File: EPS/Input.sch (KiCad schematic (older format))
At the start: 3 parts

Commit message: Updated schematics
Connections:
- wire segments 40 -> 44
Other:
- note removed: "OpAmp feedback control here (or in own sheet)"
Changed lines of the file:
@@
 LIBS:max40200
 LIBS:tps7a7002
+LIBS:max5395
 LIBS:EPS-cache
 EELAYER 25 0
@@
 S 5150 1625 1300 1150
 U 5A812530
-F0 "Boost_converters" 60
+F0 "Boost_converters with digi pot" 60
 F1 "Boost_converters.sch" 60
 F2 "BOOST1_IN" I L 5150 1775 60
@@
 Text Notes 6475 2550 0    60   ~ 0
 To ADC
-Text Notes 4900 4000 0    60   ~ 0
-OpAmp feedback control here (or in own sheet)
-Text GLabel 5000 2400 0    60   Input ~ 0
-DAC1
-Text GLabel 5000 2525 0    60   Input ~ 0
-DAC2
-Text GLabel 5000 2650 0    60   Input ~ 0
-DAC3
 Text GLabel 6575 5525 1    60   Output ~ 0
 DAC1
@@
 	5775 6450 5775 6350
 Wire Wire Line
-	5775 4625 5775 5650
+	5775 4625 5775 4950
+Wire Wire Line
+	5775 4950 5775 5350
+Wire Wire Line
+	5775 5350 5775 5650
 Wire Wire Line
 	5775 5350 5825 5350
@@
 	8625 2025 8850 2025
 Wire Wire Line
-	8850 2025 8850 1775
-Wire Wire Line
-	8625 1775 9000 1775
+	8850 2025 8850 1900
+Wire Wire Line
+	8850 1900 8850 1775
+Wire Wire Line
+	8625 1775 8850 1775
+Wire Wire Line
+	8850 1775 9000 1775
 Connection ~ 8850 1775
 Wire Wire Line
 	8625 1900 8850 1900
 Connection ~ 8850 1900
-Wire Notes Line
-	4850 2825 4850 3700
-Wire Notes Line
-	4850 3700 5775 3700
-Wire Notes Line
-	5775 3700 5775 3800
-Wire Notes Line
-	6850 4100 6850 5000
-Wire Notes Line
-	6850 5000 6675 5000
-Wire Notes Line
-	6675 5000 6675 5125
 $EndSCHEMATC

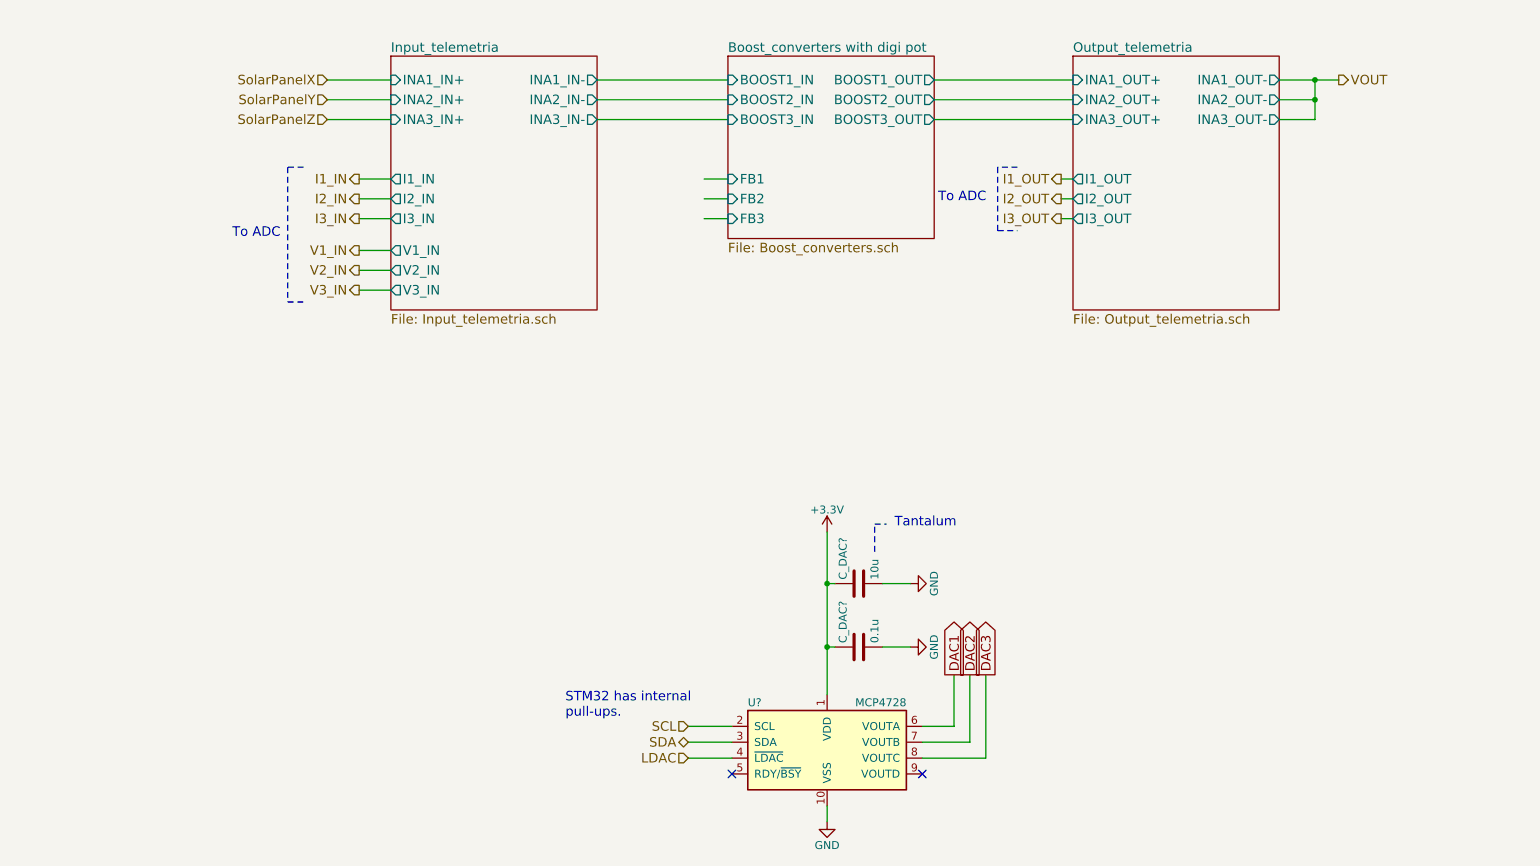
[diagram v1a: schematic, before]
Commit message: Updated Schematics
Added:
- digital pot
- digital loads
- updated  switch sheet to block two ways before battery
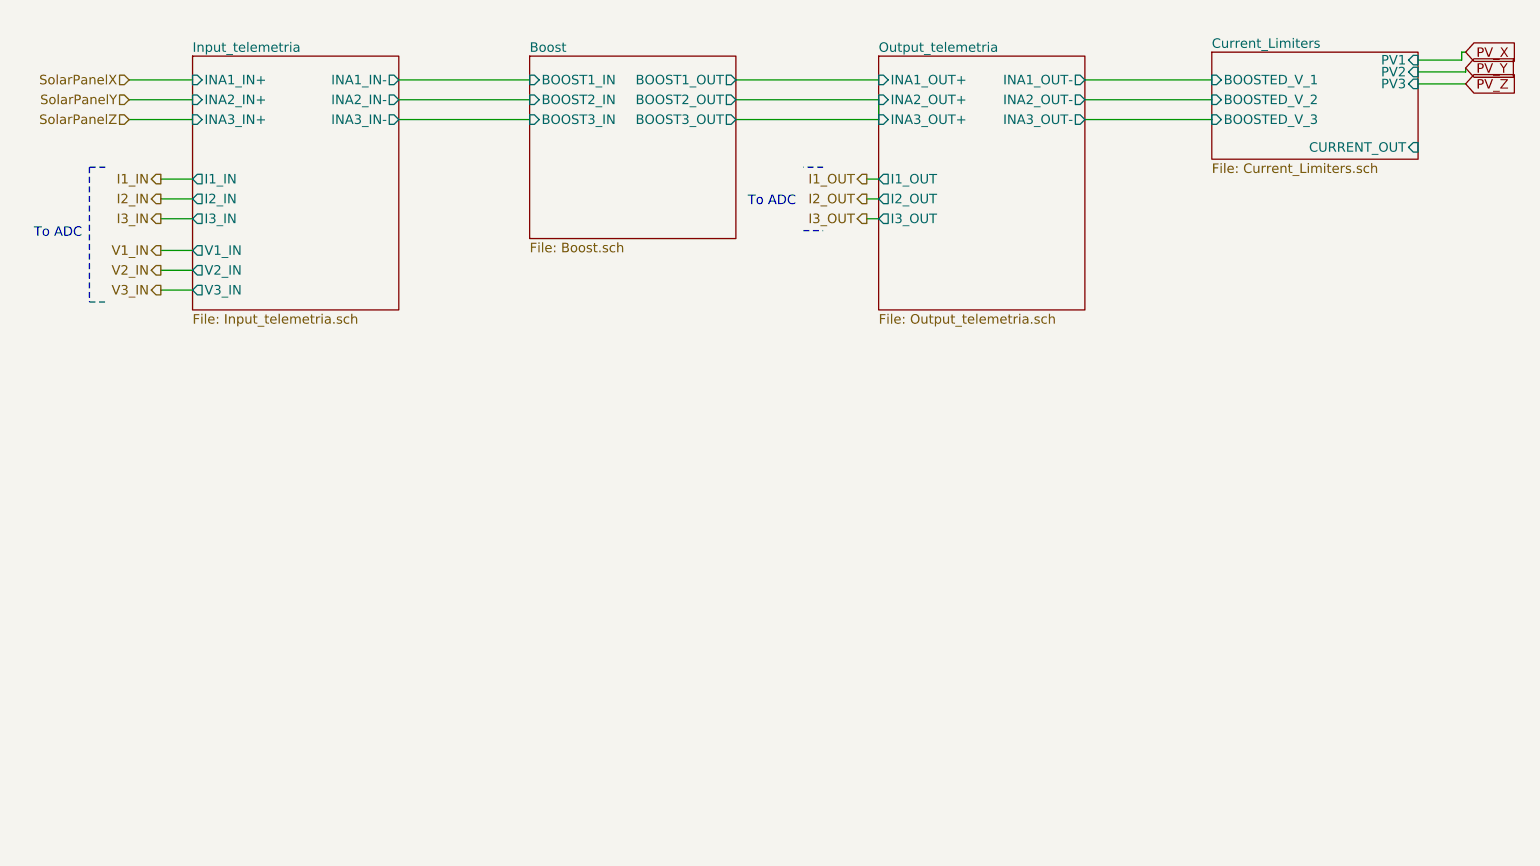
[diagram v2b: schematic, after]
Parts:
- removed C_DAC?: 10u, symbol C
- removed C_DAC?: 0.1u, symbol C
- removed U?: MCP4728, Housings_SSOP:MSOP-10_3x3mm_Pitch0.5mm, symbol MCP4728
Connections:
- net labels added: PV_X, PV_Y, PV_Z
- net labels removed: +3.3V, DAC1, DAC2, DAC3, GND, LDAC, SCL, SDA, VOUT
- wire segments 44 -> 28
- no-connect marks 2 -> 0
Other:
- note removed: "STM32 has internal\npull-ups."
- note removed: "Tantalum"

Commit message: Finalized SCH (beta version) and started pcb
Capacitor banks might need to be reassigned to other locations.
No RBF pin on this SCH or PCB.
Battery gound deployment switch is fully mechanical (no mosfet switch on low side).
PCB of the prototype started. Main power converters and current measuring devices layed out.
SCH still requires ESD protection diodes!
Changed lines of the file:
@@
 Sheet 4 14
 Title "Input"
-Date "2018-02-13"
+Date "2018-02-22"
 Rev "R1"
 Comp ""
@@
 $EndSheet
 $Sheet
-S 3900 1625 1300 1150
+S 3900 1625 1300 975
 U 5A812530
 F0 "Boost" 60
@@
 F6 "BOOST3_IN" I L 3900 2025 60
 F7 "BOOST3_OUT" O R 5200 2025 60
+F8 "SCL" I L 3900 2425 60
+F9 "SDA" B L 3900 2300 60
 $EndSheet
 $Sheet
@@
 Text HLabel 6025 2650 0    60   Output ~ 0
 I3_OUT
-Wire Notes Line
-	1225 2325 1125 2325
-Wire Notes Line
-	1125 2325 1125 3175
-Wire Notes Line
-	1125 3175 1225 3175
-Wire Notes Line
-	5750 2325 5625 2325
-Wire Notes Line
-	5625 2725 5750 2725
-Wire Wire Line
-	3075 1775 3900 1775
-Wire Wire Line
-	3075 1900 3900 1900
-Wire Wire Line
-	3075 2025 3900 2025
-Wire Wire Line
-	1375 1775 1775 1775
-Wire Wire Line
-	1375 1900 1775 1900
-Wire Wire Line
-	1375 2025 1775 2025
-Wire Wire Line
-	1575 2400 1775 2400
-Wire Wire Line
-	1575 2525 1775 2525
-Wire Wire Line
-	1575 2650 1775 2650
-Wire Wire Line
-	1575 2850 1775 2850
-Wire Wire Line
-	1575 2975 1775 2975
-Wire Wire Line
-	1575 3100 1775 3100
-Wire Wire Line
-	6025 2400 6100 2400
-Wire Wire Line
-	6025 2525 6100 2525
-Wire Wire Line
-	6025 2650 6100 2650
-$Sheet
-S 8200 1600 1300 675
+$Sheet
+S 8200 1600 1200 1675
 U 5A8CBBB0
 F0 "Current_Limiters" 60
 F1 "Current_Limiters.sch" 60
-F2 "PV2" I R 9500 1725 60
-F3 "BOOSTED_V_2" I L 8200 1900 60
-F4 "CURRENT_OUT" I R 9500 2200 60
-F5 "PV3" I R 9500 1800 60
-F6 "BOOSTED_V_3" I L 8200 2025 60
-F7 "PV1" I R 9500 1650 60
-F8 "BOOSTED_V_1" I L 8200 1775 60
-$EndSheet
-Text GLabel 9800 1600 2    60   Input ~ 0
+F2 "BOOSTED_V_2" I L 8200 1900 60
+F3 "BOOSTED_V_3" I L 8200 2025 60
+F4 "BOOSTED_V_1" I L 8200 1775 60
+F5 "VBATT_EPS" I L 8200 2725 60
+F6 "SCL" I L 8200 3050 60
+F7 "SDA" B L 8200 2950 60
+F8 "LDAC" I L 8200 3150 60
+F9 "PV_Y" I L 8200 2350 60
+F10 "PV_Z" I L 8200 2450 60
+F11 "PV_X" I L 8200 2250 60
+F12 "V_OUT" O R 9400 1775 60
+$EndSheet
+Text Label 1450 1350 3    60   ~ 0
 PV_X
-Text GLabel 9800 1700 2    60   Input ~ 0
+Text Label 1550 1350 3    60   ~ 0
 PV_Y
-Text GLabel 9800 1800 2    60   Input ~ 0
+Text Label 1650 1350 3    60   ~ 0
 PV_Z
+Text Label 7950 2250 0    60   ~ 0
+PV_X
+Text Label 7950 2350 0    60   ~ 0
+PV_Y
+Text Label 7950 2450 0    60   ~ 0
+PV_Z
+Text HLabel 9600 1775 2    60   Output ~ 0
+VOUT
+Wire Notes Line
+	1225 2325 1125 2325
+Wire Notes Line
+	1125 2325 1125 3175
+Wire Notes Line
+	1125 3175 1225 3175
+Wire Notes Line
+	5750 2325 5625 2325
+Wire Notes Line
+	5625 2725 5750 2725
+Wire Wire Line
+	3075 1775 3900 1775
+Wire Wire Line
+	3075 1900 3900 1900
+Wire Wire Line
+	3075 2025 3900 2025
+Wire Wire Line
+	1375 1775 1775 1775
+Wire Wire Line
+	1375 1900 1775 1900
+Wire Wire Line
+	1375 2025 1775 2025
+Wire Wire Line
+	1575 2400 1775 2400
+Wire Wire Line
+	1575 2525 1775 2525
+Wire Wire Line
+	1575 2650 1775 2650
+Wire Wire Line
+	1575 2850 1775 2850
+Wire Wire Line
+	1575 2975 1775 2975
+Wire Wire Line
+	1575 3100 1775 3100
+Wire Wire Line
+	6025 2400 6100 2400
+Wire Wire Line
+	6025 2525 6100 2525
+Wire Wire Line
+	6025 2650 6100 2650
 Wire Wire Line
 	5200 1775 6100 1775
@@
 	6100 2025 5200 2025
 Wire Wire Line
-	9800 1800 9500 1800
-Wire Wire Line
-	9500 1725 9800 1725
-Wire Wire Line
-	9800 1725 9800 1700
-Wire Wire Line
-	9500 1650 9775 1650
-Wire Wire Line
-	9775 1650 9775 1600
-Wire Wire Line
-	9775 1600 9800 1600
-Wire Wire Line
 	7400 1775 8200 1775
 Wire Wire Line
@@
 Wire Wire Line
 	7400 2025 8200 2025
+Wire Wire Line
+	1450 1775 1450 1350
+Connection ~ 1450 1775
+Wire Wire Line
+	1550 1900 1550 1350
+Connection ~ 1550 1900
+Wire Wire Line
+	1650 2025 1650 1350
+Connection ~ 1650 2025
+Wire Wire Line
+	7950 2250 8200 2250
+Wire Wire Line
+	7950 2350 8200 2350
+Wire Wire Line
+	7950 2450 8200 2450
+Wire Wire Line
+	9600 1775 9400 1775
+Text HLabel 8025 2950 0    60   BiDi ~ 0
+SDA
+Wire Wire Line
+	8025 2950 8200 2950
+Text HLabel 8025 3050 0    60   Input ~ 0
+SCL
+Wire Wire Line
+	8025 3050 8200 3050
+Text HLabel 8025 3150 0    60   Input ~ 0
+LDAC
+Wire Wire Line
+	8025 3150 8200 3150
+Text HLabel 3725 2300 0    60   BiDi ~ 0
+SDA
+Wire Wire Line
+	3725 2300 3900 2300
+Text HLabel 3725 2425 0    60   BiDi ~ 0
+SCL
+Wire Wire Line
+	3725 2425 3900 2425
+Text HLabel 8025 2725 0    60   Input ~ 0
+VBATT_EPS
+Wire Wire Line
+	8025 2725 8200 2725
 $EndSCHEMATC
